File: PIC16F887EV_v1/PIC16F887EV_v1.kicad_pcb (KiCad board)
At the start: 2 copper layers, 100 x 100 mm, 101 parts, among them J1 USB_C_Receptacle_USB2.0_14P, Q1 2N3904, Q2 2N3904, Q3 2N3904, Q5 2N3904, SW1 SW_Push, SW10 SW_Push, SW11 SW_Push, SW12 SW_Push, SW13 SW_Push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

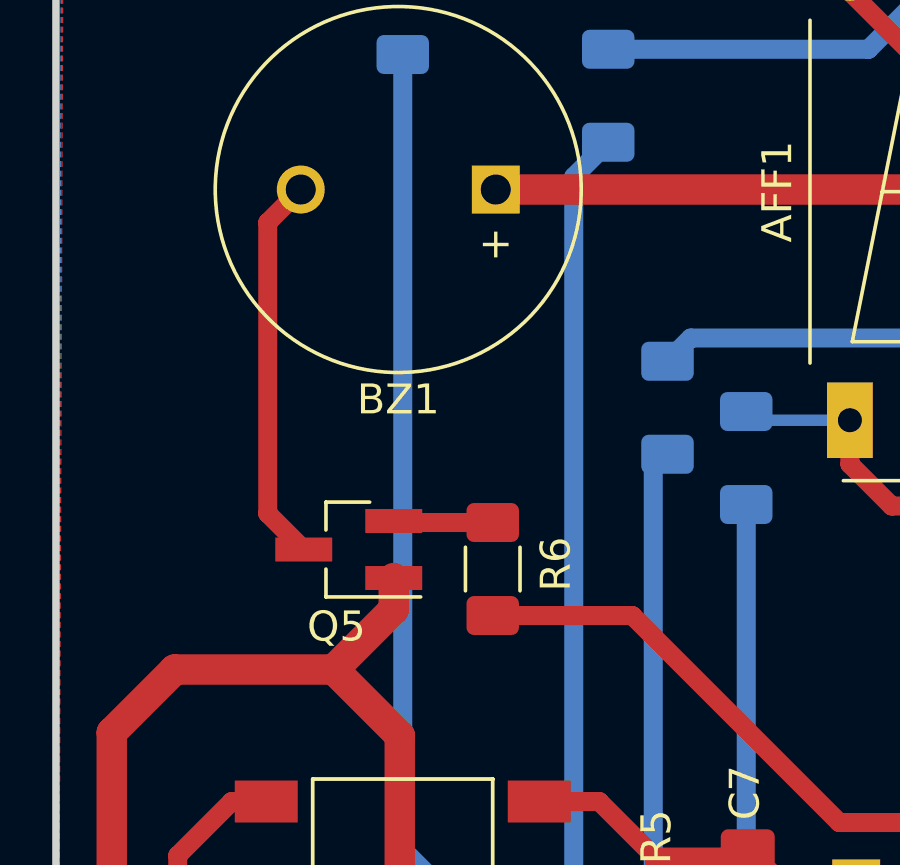
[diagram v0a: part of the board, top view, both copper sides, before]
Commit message: Correccion errores v1, y finalizacion V2
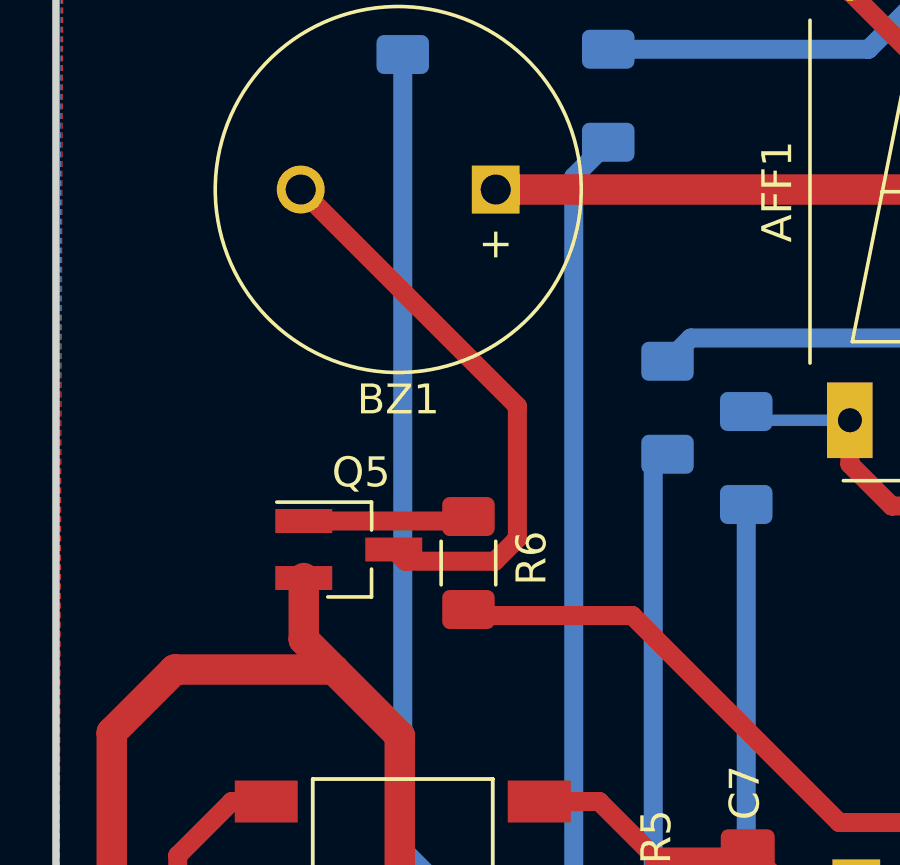
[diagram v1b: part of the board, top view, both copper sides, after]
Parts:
- moved R6 0.83 mm to (29.0, 43.5)
- turned Q5 to 0 degrees
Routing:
- net Net-(BZ1-+): track 13.0 -> 19.2 mm
- net Net-(Q5-B): track 3.82 -> 5.55 mm
- net RA4: track 29.2 -> 30.0 mm
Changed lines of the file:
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@@
 		(fp_arc
 			(start -2.1747 0.3223)
-			(mid -1.600348 -4.921578)
+			(mid -1.600349 -4.921577)
 			(end 3.1903 -2.713)
 			(stroke
@@
 		(fp_arc
 			(start -2.1747 0.3223)
-			(mid -1.600348 -4.921578)
+			(mid -1.600349 -4.921577)
 			(end 3.1903 -2.713)
 			(stroke
@@
 	(footprint "Resistor_SMD:R_1206_3216Metric_Pad1.30x1.75mm_HandSolder"
 		(layer "F.Cu")
-		(at 29.8 43.75 -90)
+		(at 28.99 43.55 -90)
 		(descr "Resistor SMD 1206 (3216 Metric), square (rectangular) end terminal, IPC_7351 nominal with elongated pad for handsoldering. (Body size source: IPC-SM-782 page 72, https://www.pcb-3d.com/wordpress/wp-content/uploads/ipc-sm-782a_amendment_1_and_2.pdf), generated with kicad-footprint-generator")
 		(tags "resistor handsolder")
@@
 	(footprint "Huellas:SOT-23_Handsoldering-mod"
 		(layer "F.Cu")
-		(at 25 43.1 180)
+		(at 25 43.1)
 		(descr "SOT-23, Handsoldering")
 		(tags "SOT-23")
 		(property "Reference" "Q5"
-			(at 0.4128 -2.5692 180)
+			(at 0.4128 -2.5692 360)
 			(layer "F.SilkS")
 			(effects
@@
 		)
 		(property "Footprint" "Huellas:SOT-23_Handsoldering-mod"
-			(at 0 0 180)
+			(at 0 0 360)
 			(layer "B.Fab")
 			(hide yes)
@@
 		)
 		(property "Datasheet" "https://www.onsemi.com/pub/Collateral/2N3903-D.PDF"
-			(at 0 0 180)
+			(at 0 0 360)
 			(layer "B.Fab")
 			(hide yes)
@@
 		)
 		(property "Description" ""
-			(at 0 0 180)
+			(at 0 0 360)
 			(layer "B.Fab")
 			(hide yes)
@@
 		(attr smd)
 		(fp_line
-			(start 0.76 0.65)
-			(end 0.76 1.58)
+			(start -2.4 -1.58)
+			(end 0.76 -1.58)
 			(stroke
 				(width 0.12)
@@
 		)
 		(fp_line
-			(start 0.76 -0.65)
-			(end 0.76 -1.58)
+			(start -0.7 1.58)
+			(end 0.76 1.58)
 			(stroke
 				(width 0.12)
@@
 		)
 		(fp_line
-			(start -0.7 1.58)
-			(end 0.76 1.58)
+			(start 0.76 -0.65)
+			(end 0.76 -1.58)
 			(stroke
 				(width 0.12)
@@
 		)
 		(fp_line
-			(start -2.4 -1.58)
-			(end 0.76 -1.58)
+			(start 0.76 0.65)
+			(end 0.76 1.58)
 			(stroke
 				(width 0.12)
@@
 		)
 		(fp_line
-			(start 2.7 1.75)
-			(end 2.7 -1.75)
+			(start -2.7 -1.75)
+			(end -2.7 1.75)
 			(stroke
 				(width 0.05)
@@
 		)
 		(fp_line
-			(start 2.7 -1.75)
-			(end -2.7 -1.75)
+			(start -2.7 1.75)
+			(end 2.7 1.75)
 			(stroke
 				(width 0.05)
@@
 		)
 		(fp_line
-			(start -2.7 1.75)
-			(end 2.7 1.75)
+			(start 2.7 -1.75)
+			(end -2.7 -1.75)
 			(stroke
 				(width 0.05)
@@
 		)
 		(fp_line
-			(start -2.7 -1.75)
-			(end -2.7 1.75)
+			(start 2.7 1.75)
+			(end 2.7 -1.75)
 			(stroke
 				(width 0.05)
@@
 		)
 		(fp_line
-			(start 0.7 1.52)
-			(end 0.7 -1.52)
+			(start -0.7 1.5)
+			(end -0.7 -0.95)
 			(stroke
 				(width 0.1)
@@
 		)
 		(fp_line
-			(start 0.7 1.52)
-			(end -0.7 1.52)
+			(start -0.15 -1.52)
+			(end -0.7 -0.95)
 			(stroke
 				(width 0.1)
@@
 		)
 		(fp_line
-			(start -0.15 -1.52)
-			(end -0.7 -0.95)
+			(start 0.7 1.52)
+			(end -0.7 1.52)
 			(stroke
 				(width 0.1)
@@
 		)
 		(fp_line
-			(start -0.7 1.5)
-			(end -0.7 -0.95)
+			(start 0.7 1.52)
+			(end 0.7 -1.52)
 			(stroke
 				(width 0.1)
@@
 		)
 		(pad "1" smd rect
-			(at -1.5 0.95 180)
+			(at -1.5 0.95)
 			(size 1.9 0.8)
 			(layers "F.Cu" "F.Paste" "F.Mask")
@@
 		)
 		(pad "2" smd rect
-			(at -1.5 -0.95 180)
+			(at -1.5 -0.95)
 			(size 1.9 0.8)
 			(layers "F.Cu" "F.Paste" "F.Mask")
@@
 		)
 		(pad "3" smd rect
-			(at 1.5 0 180)
+			(at 1.5 0)
 			(size 1.9 0.8)
 			(layers "F.Cu" "F.Paste" "F.Mask")
@@
 		)
 	)
+	(gr_text "SPI"
+		(at 105.7 64.8 0)
+		(layer "F.Mask")
+		(effects
+			(font
+				(size 2.032 2.032)
+				(thickness 0.508)
+				(bold yes)
+			)
+			(justify left bottom)
+		)
+	)
 	(gr_text "1"
 		(at 49.95 81.75 0)
@@
 		)
 	)
+	(gr_text "USART"
+		(at 103.3 76 0)
+		(layer "F.Mask")
+		(effects
+			(font
+				(size 2.032 2.032)
+				(thickness 0.508)
+				(bold yes)
+			)
+			(justify left bottom)
+		)
+	)
 	(gr_text "2"
 		(at 65.15 81.7 0)
@@
 	)
 	(segment
-		(start 23.5 43.1)
-		(end 22.3 41.9)
+		(start 26.5 43.1)
+		(end 26.89 43.49)
 		(width 0.635)
 		(layer "F.Cu")
@@
 	)
 	(segment
-		(start 22.3 41.9)
-		(end 22.3 32.2)
+		(start 30.62 42.74)
+		(end 30.62 38.32)
 		(width 0.635)
 		(layer "F.Cu")
@@
 	)
 	(segment
-		(start 22.3 32.2)
+		(start 30.62 38.32)
 		(end 23.4 31.1)
 		(width 0.635)
@@
 	)
 	(segment
-		(start 53 52.2)
-		(end 41.35 52.2)
+		(start 29.87 43.49)
+		(end 30.62 42.74)
 		(width 0.635)
 		(layer "F.Cu")
-		(net 6)
+		(net 5)
 	)
 	(segment
-		(start 41.35 52.2)
-		(end 34.45 45.3)
+		(start 26.89 43.49)
+		(end 29.87 43.49)
+		(width 0.635)
+		(layer "F.Cu")
+		(net 5)
+	)
+	(segment
+		(start 29.19 45.3)
+		(end 28.99 45.1)
 		(width 0.635)
 		(layer "F.Cu")
@@
 	(segment
 		(start 34.45 45.3)
-		(end 29.8 45.3)
+		(end 29.19 45.3)
 		(width 0.635)
 		(layer "F.Cu")
@@
 	)
 	(segment
-		(start 54.615 54.63)
-		(end 54.615 53.815)
+		(start 53 52.2)
+		(end 41.35 52.2)
+		(width 0.635)
+		(layer "F.Cu")
+		(net 6)
+	)
+	(segment
+		(start 41.35 52.2)
+		(end 34.45 45.3)
 		(width 0.635)
 		(layer "F.Cu")
@@
 	)
 	(segment
+		(start 54.615 54.63)
+		(end 54.615 53.815)
+		(width 0.635)
+		(layer "F.Cu")
+		(net 6)
+	)
+	(segment
 		(start 61.075 45.775)
 		(end 61.1 45.8)
@@
 	)
 	(segment
+		(start 23.5 46.1)
+		(end 23.5 44.05)
+		(width 1.016)
+		(layer "F.Cu")
+		(net 10)
+	)
+	(segment
 		(start 41.95 99.05)
 		(end 42.1 98.9)
@@
 	)
 	(segment
-		(start 26.5 45.1)
-		(end 26.5 44.05)
-		(width 1.016)
-		(layer "F.Cu")
-		(net 10)
-	)
-	(segment
 		(start 41.5 89.5)
 		(end 42.1 88.9)
@@
 	)
 	(segment
+		(start 24.5 47.1)
+		(end 23.5 46.1)
+		(width 1.016)
+		(layer "F.Cu")
+		(net 10)
+	)
+	(segment
 		(start 17.35 86.75)
 		(end 17.3 86.7)
@@
 	)
 	(segment
-		(start 24.5 47.1)
-		(end 26.5 45.1)
-		(width 1.016)
-		(layer "F.Cu")
-		(net 10)
-	)
-	(segment
 		(start 42.1 108.8)
 		(end 42.1 112.85)
@@
 	)
 	(segment
-		(start 26.55 42.2)
-		(end 26.5 42.15)
-		(width 0.635)
-		(layer "F.Cu")
-		(net 70)
-	)
-	(segment
-		(start 29.8 42.2)
-		(end 26.55 42.2)
+		(start 28.84 42.15)
+		(end 28.99 42)
 		(width 0.635)
 		(layer "F.Cu")
@@
 	)
 	(segment
-		(start 27 42.15)
-		(end 26.5 42.15)
+		(start 23.5 42.15)
+		(end 28.84 42.15)
 		(width 0.635)
 		(layer "F.Cu")
